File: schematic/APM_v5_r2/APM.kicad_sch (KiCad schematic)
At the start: 27 parts, among them J10 Conn_02x17_Counter_Clockwise, J14 POT_FFC, J18 CTRL_FFC, J2 CAN, J4 LCD_display, J6 Conn_02x10_Counter_Clockwise, J8 Conn_02x15_Counter_Clockwise, J9 Conn_02x08_Counter_Clockwise

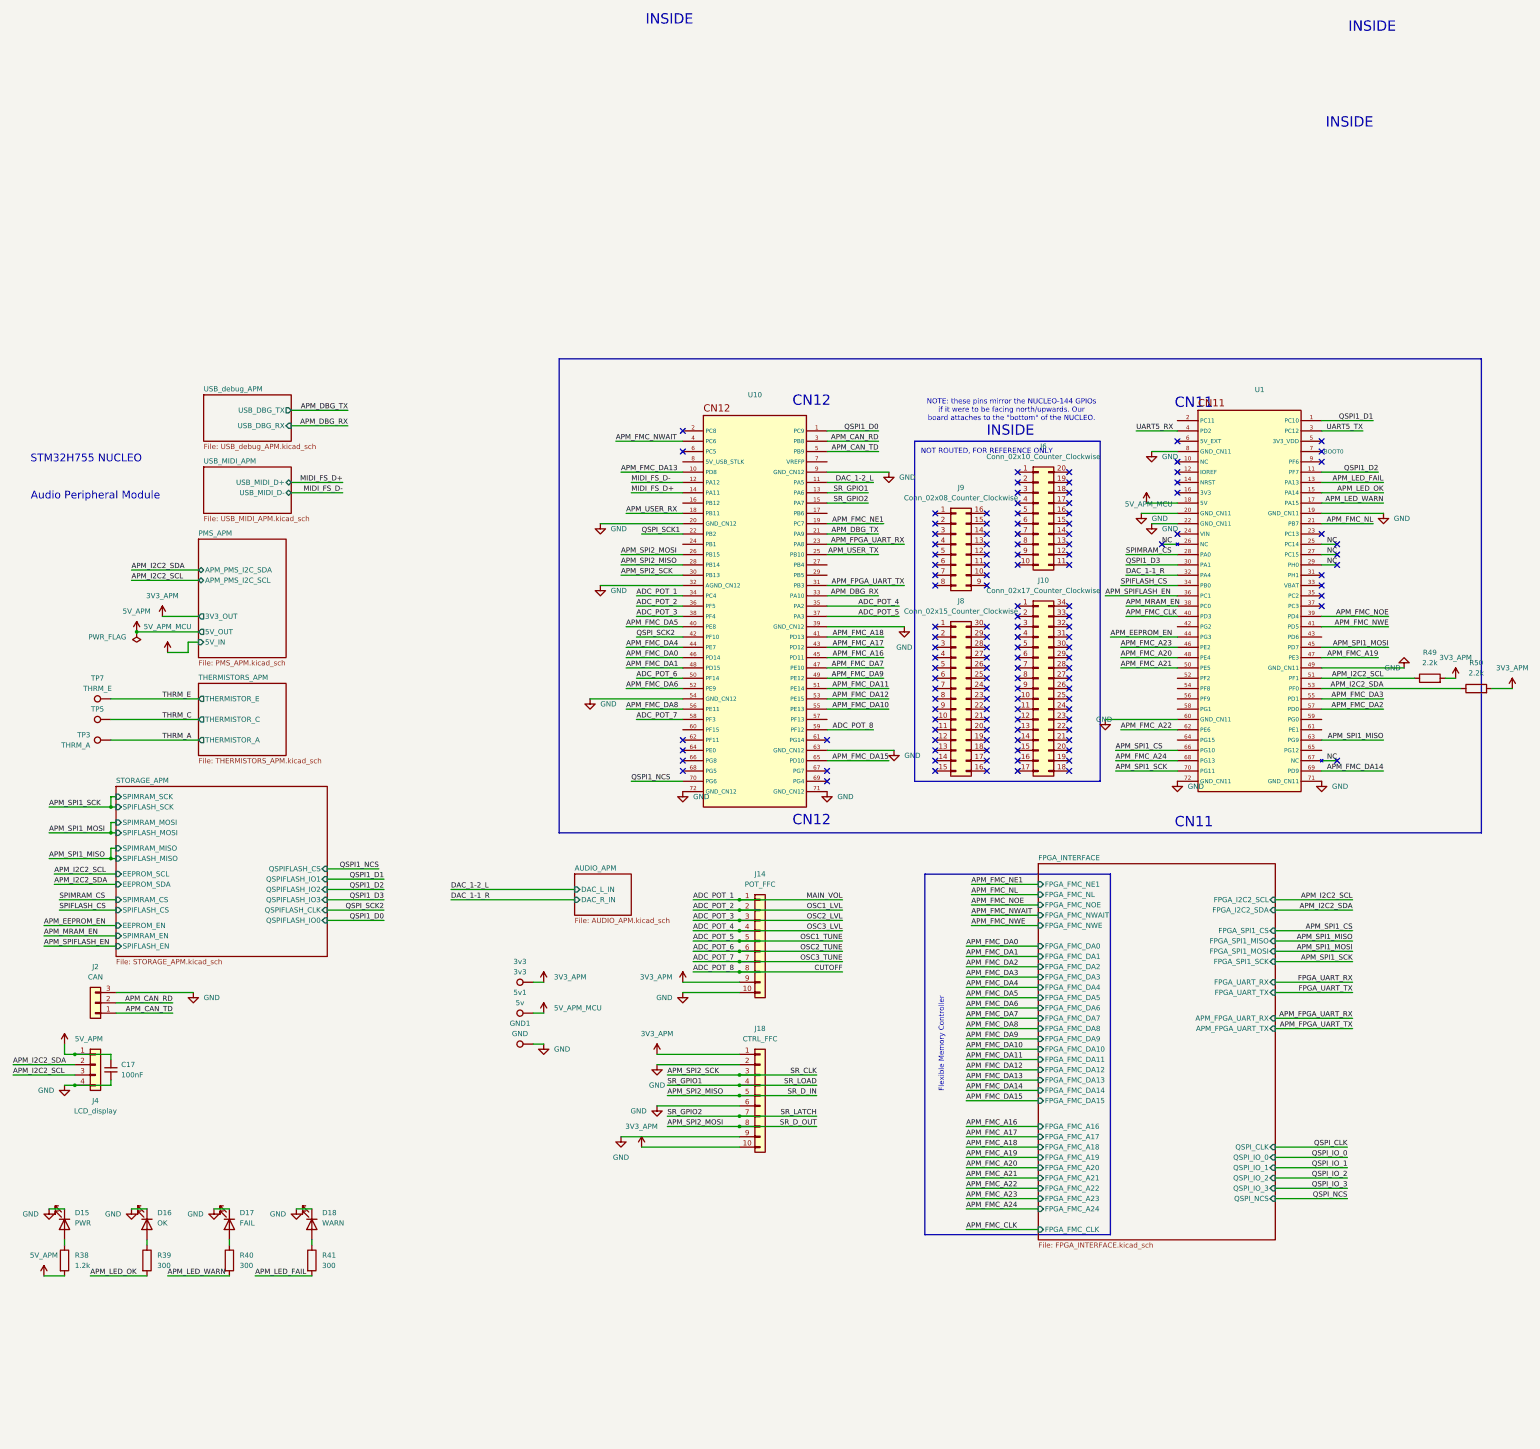
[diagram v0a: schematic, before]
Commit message: adding new rev of apm board with new routing and power management
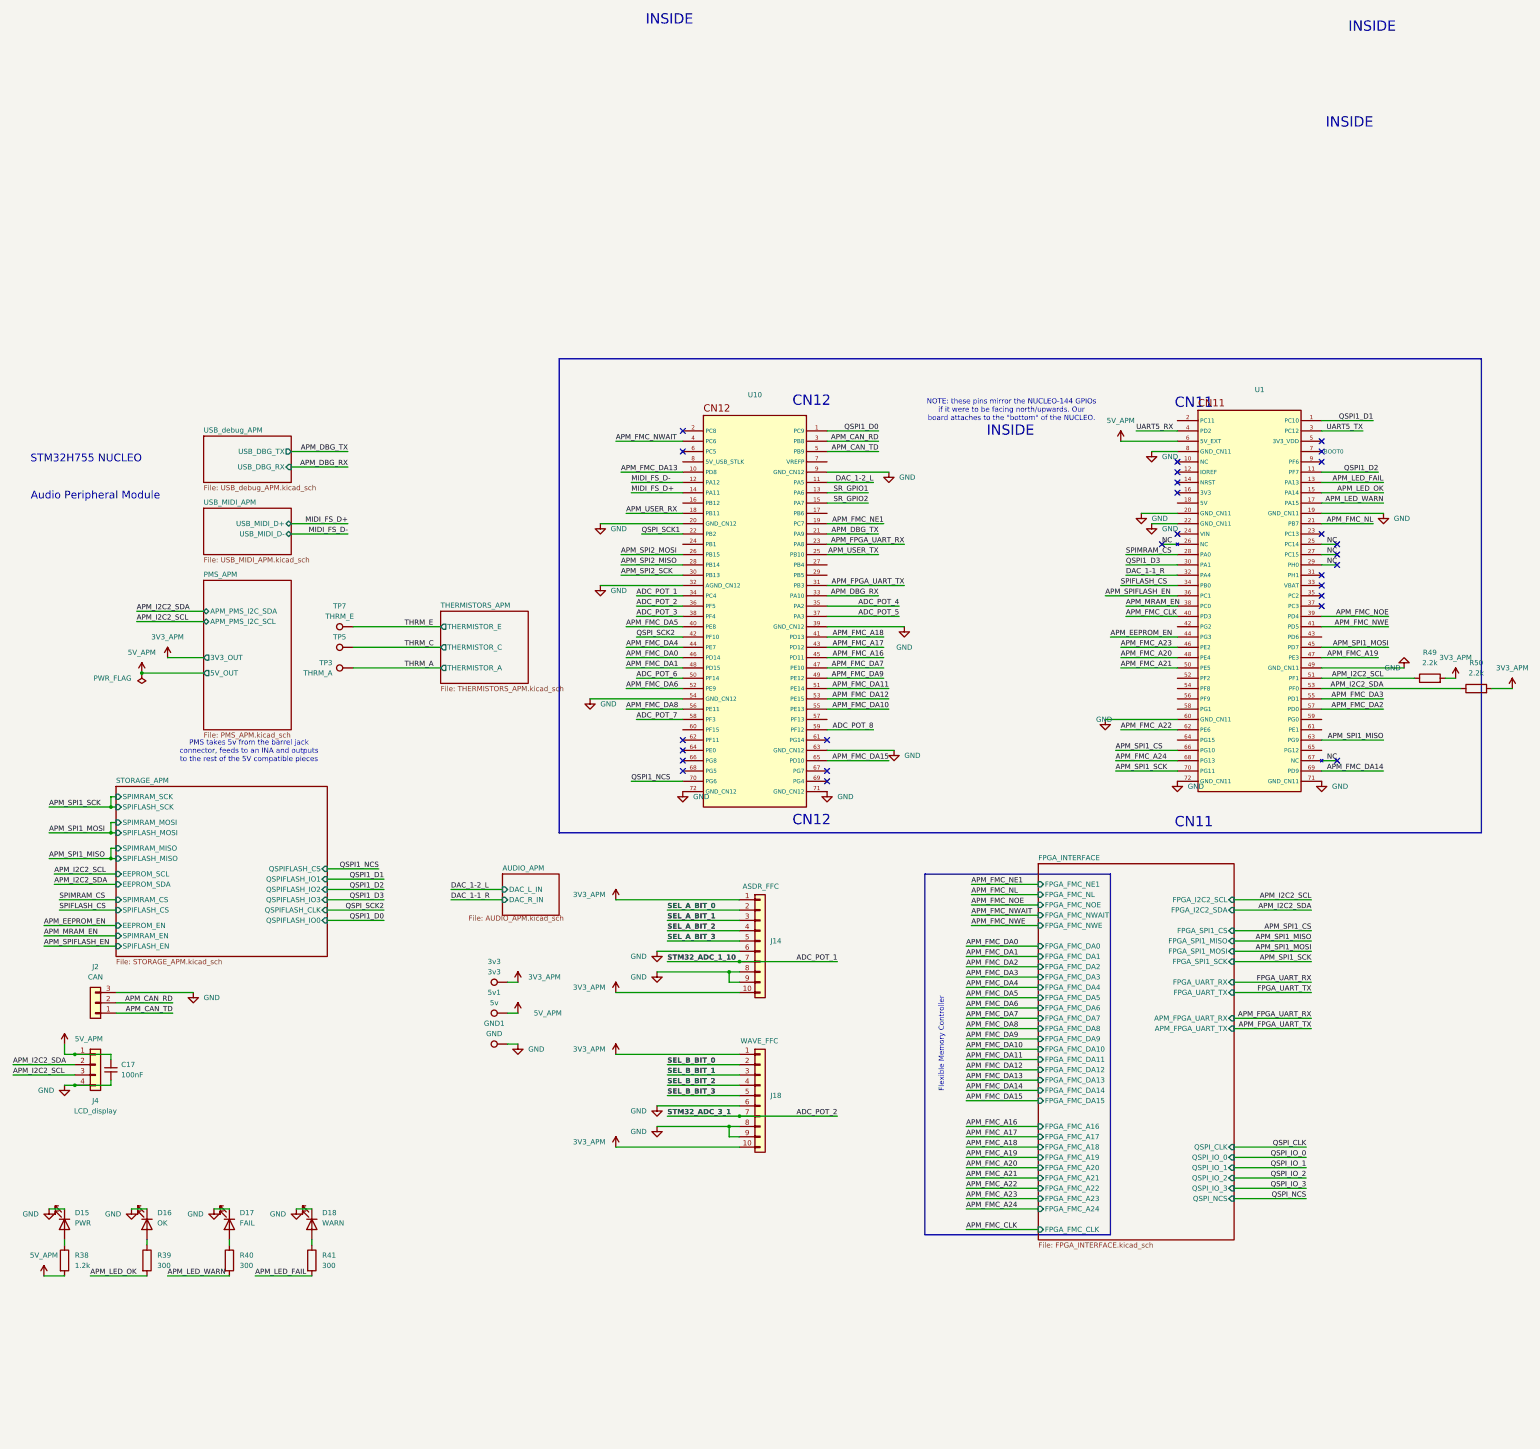
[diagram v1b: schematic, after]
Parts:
- removed J10: Conn_02x17_Counter_Clockwise, symbol Connector_Generic:Conn_02x17_Counter_Clockwise
- removed J6: Conn_02x10_Counter_Clockwise, symbol Connector_Generic:Conn_02x10_Counter_Clockwise
- removed J8: Conn_02x15_Counter_Clockwise, symbol Connector_Generic:Conn_02x15_Counter_Clockwise
- removed J9: Conn_02x08_Counter_Clockwise, symbol Connector_Generic:Conn_02x08_Counter_Clockwise
- J14: value POT_FFC -> ASDR_FFC
- J18: value CTRL_FFC -> WAVE_FFC
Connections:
- net 3V3_APM: now also J14.1 (Pin_1), J14.10 (Pin_10); no longer J14.9 (Pin_9)
- net 5V_APM: now also 5v1.1, U1.6 (5V_EXT)
- net ADC_POT_1: now also J14.7 (Pin_7); no longer J14.1 (Pin_1)
- net ADC_POT_2: now also J18.7 (Pin_7); no longer J14.2 (Pin_2)
- net ADC_POT_3: no longer J14.3 (Pin_3)
- net ADC_POT_4: no longer J14.4 (Pin_4)
- net ADC_POT_5: no longer J14.5 (Pin_5)
- net ADC_POT_6: no longer J14.6 (Pin_6)
- net ADC_POT_7: no longer J14.7 (Pin_7)
- net ADC_POT_8: no longer J14.8 (Pin_8)
- net APM_SPI2_MISO: no longer J18.5 (Pin_5)
- net APM_SPI2_MOSI: no longer J18.8 (Pin_8)
- net APM_SPI2_SCK: no longer J18.3 (Pin_3)
- net GND: now also J14.6 (Pin_6), J14.8 (Pin_8), J14.9 (Pin_9), J18.8 (Pin_8); no longer J14.10 (Pin_10), J18.2 (Pin_2)
- net SR_GPIO1: no longer J18.4 (Pin_4)
- net SR_GPIO2: no longer J18.7 (Pin_7)
- net 5V_APM_MCU: no longer names the net of U1.18 (5V)
- net 5V_APM_MCU: no longer 5v1.1
- new net SEL_A_BIT_0: J14.2 (Pin_2)
- new net SEL_A_BIT_1: J14.3 (Pin_3)
- new net SEL_A_BIT_2: J14.4 (Pin_4)
- new net SEL_A_BIT_3: J14.5 (Pin_5)
- new net SEL_B_BIT_0: J18.2 (Pin_2)
- new net SEL_B_BIT_1: J18.3 (Pin_3)
- new net SEL_B_BIT_2: J18.4 (Pin_4)
- new net SEL_B_BIT_3: J18.5 (Pin_5)
- no-connect marks 128 -> 27
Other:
- sheet PMS_APM ports: added none; removed 5V_IN
- note added: "PMS takes 5v from the barrel jack connector, feeds to an INA and outputs to the rest of the 5V compatible pieces"
- note removed: "NOT ROUTED, FOR REFERENCE ONLY"
- moved on the sheet: 3v3, 5v1, GND1, TP3, TP5, TP7

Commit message: trying APM placement
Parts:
- removed J14: ASDR_FFC, Connector_FFC-FPC:Hirose_FH12-10S-0.5SH_1x10-1MP_P0.50mm_Horizontal, symbol Connector_Generic:Conn_01x10
- removed J18: WAVE_FFC, Connector_FFC-FPC:Hirose_FH12-10S-0.5SH_1x10-1MP_P0.50mm_Horizontal, symbol Connector_Generic:Conn_01x10
- added J6: OSC_CTRL, my_footprints:GCT_FFC2B28-20-G, symbol FFC2B28-20-G:FFC2B28-20-G
- added TP4: FPC_3V3_TP, TestPoint:TestPoint_Pad_D1.0mm, symbol Connector:TestPoint
- added TP9: FPC_GND_TP, TestPoint:TestPoint_Pad_D1.0mm, symbol Connector:TestPoint
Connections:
- net 3V3_APM: now also J6.19, J6.9, TP4.1
- net ADC_POT_1: now also J6.7
- net ADC_POT_2: now also J6.17
- net GND: now also J6.1, J6.10, J6.11, J6.16, J6.18, J6.20, J6.6, J6.8, J6.S1 (SHIELD), J6.S2 (SHIELD), TP9.1
- net SEL_A_BIT_0: now also J6.2
- net SEL_A_BIT_1: now also J6.3
- net SEL_A_BIT_2: now also J6.4
- net SEL_A_BIT_3: now also J6.5
- net SEL_B_BIT_0: now also J6.12
- net SEL_B_BIT_1: now also J6.13
- net SEL_B_BIT_2: now also J6.14
- net SEL_B_BIT_3: now also J6.15
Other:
- note added: "ASDR"
- note added: "Each pad is capable of supplying 0.5A"
- note added: "WAVE_SEL"

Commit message: renders. APM V5 R2 placement. going on with routing
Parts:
- removed J2: CAN, Connector_PinHeader_2.54mm:PinHeader_1x03_P2.54mm_Vertical, symbol Connector_Generic:Conn_01x03
- TP3, TP5, TP7: footprint TestPoint:TestPoint_Pad_1.5x1.5mm -> TestPoint:TestPoint_Pad_D1.0mm
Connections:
- net SR_GPIO1 is gone; now on net SEL_B_BIT_2: U10.13 (PA6)
- net SR_GPIO2 is gone; now on net SEL_B_BIT_3: U10.15 (PA7)
- net APM_LED_FAIL: now also R40.2, U10.66 (PG8); no longer R41.2, U1.13 (PA13)
- net APM_LED_OK: now also U10.68 (PG5); no longer U1.15 (PA14)
- net APM_LED_WARN: now also R41.2, U10.64 (PE0); no longer R40.2, U1.17 (PA15)
- net SEL_A_BIT_0: now also U10.27 (PB4)
- net SEL_A_BIT_1: now also U10.29 (PB5)
- net SEL_A_BIT_2: now also U10.24 (PB1)
- net SEL_A_BIT_3: now also U10.17 (PB6)
- net SEL_B_BIT_0: now also U10.16 (PB12)
- net SEL_B_BIT_1: now also U10.60 (PF15)
- no-connect marks 27 -> 24

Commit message: routed and passing DRC except for the differentials for USB
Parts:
- J4: footprint Connector_PinHeader_2.54mm:PinHeader_1x04_P2.54mm_Vertical -> Connector_PinHeader_2.54mm:PinHeader_1x04_P2.54mm_Vertical_SMD_Pin1Left
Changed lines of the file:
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@@
 			)
 		)
-		(property "Footprint" "Connector_PinHeader_2.54mm:PinHeader_1x04_P2.54mm_Vertical"
+		(property "Footprint" "Connector_PinHeader_2.54mm:PinHeader_1x04_P2.54mm_Vertical_SMD_Pin1Left"
 			(at 44.45 182.88 0)
 			(hide yes)

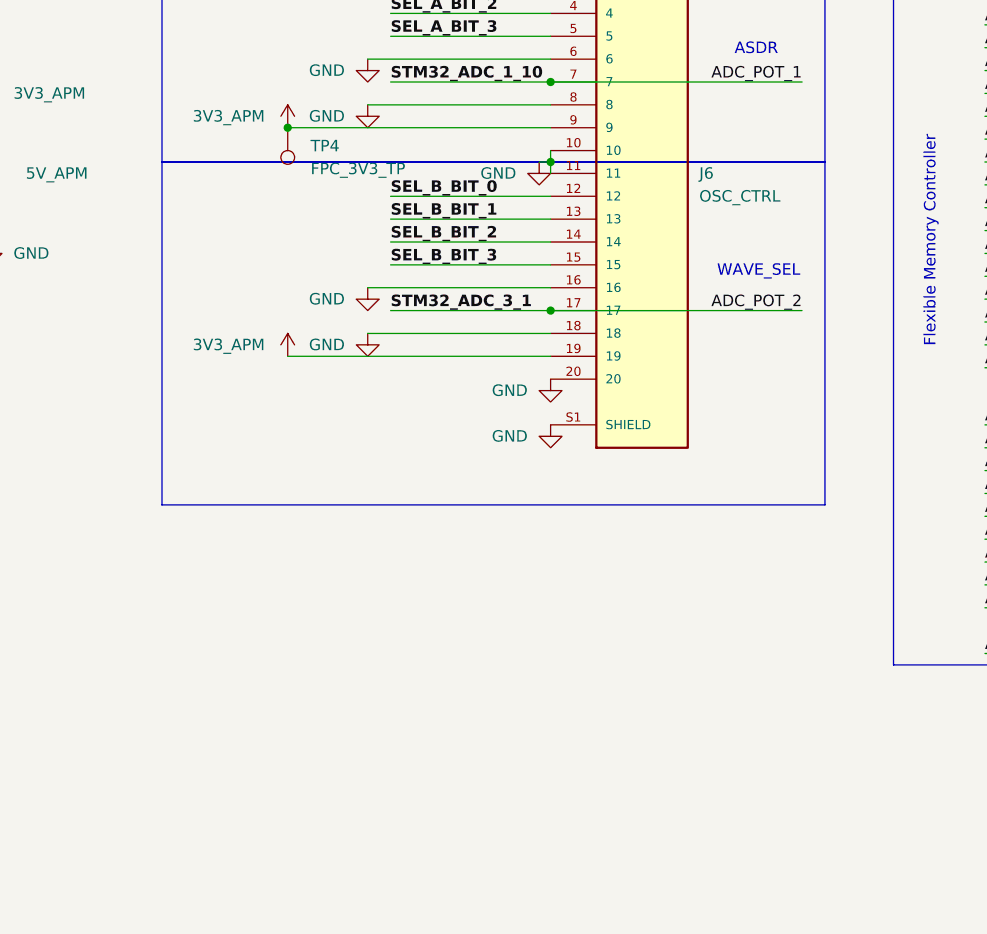
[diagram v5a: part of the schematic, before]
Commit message: working on new APM board to send out. needs FFC interface to a new audio ctrl board im making. 4p FFC for power. 10p FFC for control
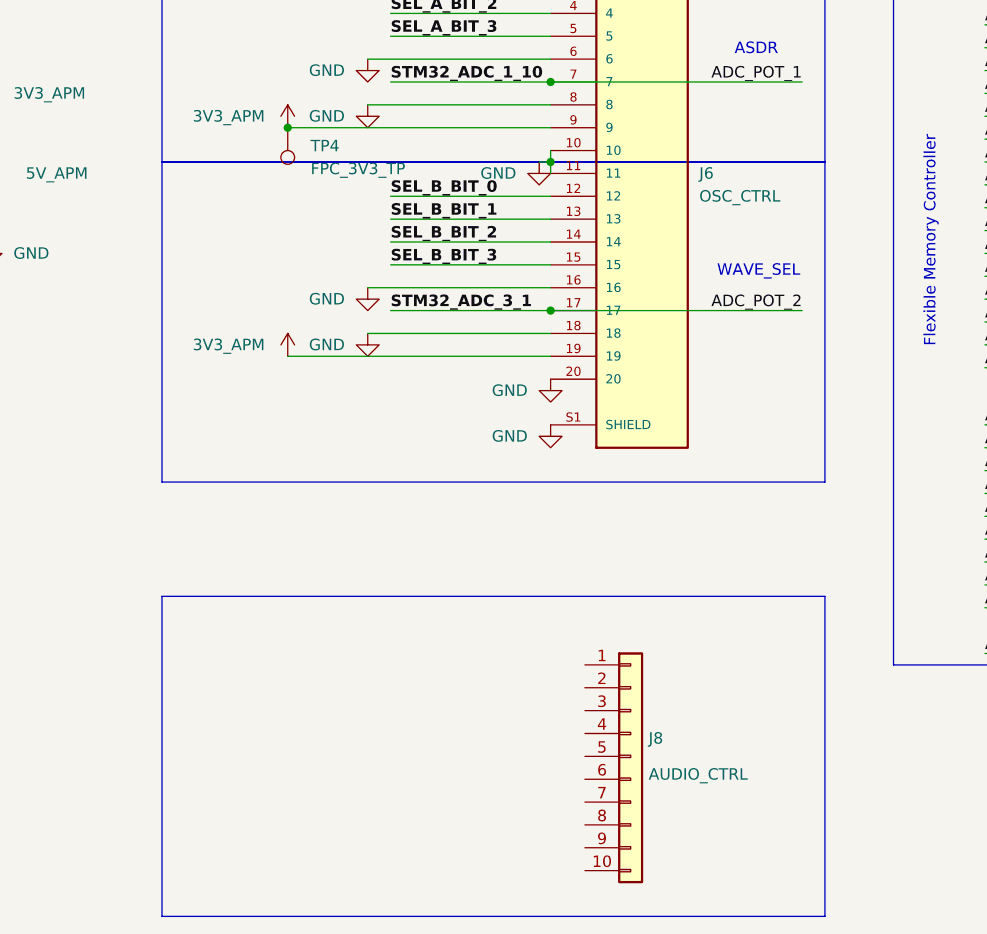
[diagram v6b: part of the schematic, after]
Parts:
- added J8: AUDIO_CTRL, Connector_FFC-FPC:Hirose_FH12-10S-0.5SH_1x10-1MP_P0.50mm_Horizontal, symbol Connector_Generic:Conn_01x10
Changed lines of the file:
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@@
 	(rectangle
 		(start 167.64 168.91)
-		(end 241.3 207.01)
+		(end 241.3 204.47)
+		(stroke
+			(width 0)
+			(type solid)
+		)
+		(fill
+			(type color)
+			(color 251 198 255 1)
+		)
+	)
+	(rectangle
+		(start 167.64 217.17)
+		(end 241.3 252.73)
 		(stroke
 			(width 0)
@@
 					(unit 1)
 				)
+			)
+		)
+	)
+	(symbol
+		(lib_id "Connector_Generic:Conn_01x10")
+		(at 219.71 234.95 0)
+		(unit 1)
+		(body_style 1)
+		(exclude_from_sim no)
+		(in_bom yes)
+		(on_board yes)
+		(in_pos_files yes)
+		(dnp no)
+		(property "Reference" "J8"
+			(at 221.71 232.95 0)
+			(show_name no)
+			(do_not_autoplace no)
+			(effects
+				(font
+					(size 1.27 1.27)
+				)
+				(justify left)
+			)
+		)
+		(property "Value" "AUDIO_CTRL"
+			(at 221.71 236.95 0)
+			(show_name no)
+			(do_not_autoplace no)
+			(effects
+				(font
+					(size 1.27 1.27)
+				)
+				(justify left)
+			)
+		)
+		(property "Footprint" "Connector_FFC-FPC:Hirose_FH12-10S-0.5SH_1x10-1MP_P0.50mm_Horizontal"
+			(at 219.71 234.95 0)
+			(hide yes)
+			(show_name no)
+			(do_not_autoplace no)
+			(effects
+				(font
+					(size 1.27 1.27)
+				)
+			)
+		)
+		(property "Datasheet" ""
+			(at 219.71 234.95 0)
+			(show_name no)
+			(do_not_autoplace no)
+			(effects
+				(font
+					(size 1.27 1.27)
+				)
+			)
+		)
+		(property "Description" ""
+			(at 219.71 234.95 0)
+			(show_name no)
+			(do_not_autoplace no)
+			(effects
+				(font
+					(size 1.27 1.27)
+				)
+			)
+		)
+		(pin "6"
+		)
+		(pin "7"
+		)
+		(pin "8"
+		)
+		(pin "1"
+		)
+		(pin "2"
+		)
+		(pin "3"
+		)
+		(pin "4"
+		)
+		(pin "5"
+		)
+		(pin "9"
+		)
+		(pin "10"
+		)
+		(instances
+			(project "APM"
+				(path "/63e257c1-2fa4-4533-ab9e-932d24befb8c"
+					(reference "J8")
+					(unit 1)
+				)

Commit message: osc ctrl has black mask, sent to JLCPCB. APM routed. also sent to JLCPCB.figuring out the master audio control board
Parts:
- added J2: AUDIO_PWR, my_footprints:AMPHENOL_F3311A7H121004E200, symbol F3311A7H121004E200:F3311A7H121004E200
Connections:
- net 5V_APM: now also J2.1, J2.2
- net APM_SPI2_MISO: now also J8.3 (Pin_3)
- net APM_SPI2_MOSI: now also J8.2 (Pin_2)
- net APM_SPI2_SCK: now also J8.1 (Pin_1)
- net GND: now also J8.8 (Pin_8), J8.9 (Pin_9), J2.3, J2.4
- net AUD_SPARE: now reaches J8.10 (Pin_10)
- net AUD_SPARE: now also U1.58 (PG1)
- net AUD_CS_DAC: now reaches J8.4 (Pin_4)
- net AUD_CS_DAC: now also U1.43 (PD6)
- net AUD_CS_POTS: now reaches J8.5 (Pin_5)
- net AUD_CS_POTS: now also U1.52 (PF2)
- net AUD_MODE: now reaches J8.6 (Pin_6)
- net AUD_MODE: now also U1.42 (PG2)
- net AUD_GATE: now reaches J8.7 (Pin_7)
- net AUD_GATE: now also U1.59 (PG0)
